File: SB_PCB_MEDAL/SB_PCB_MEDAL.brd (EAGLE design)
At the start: 60 x 60 mm, 9 parts, among them IC1 ATTINY44A-SSU

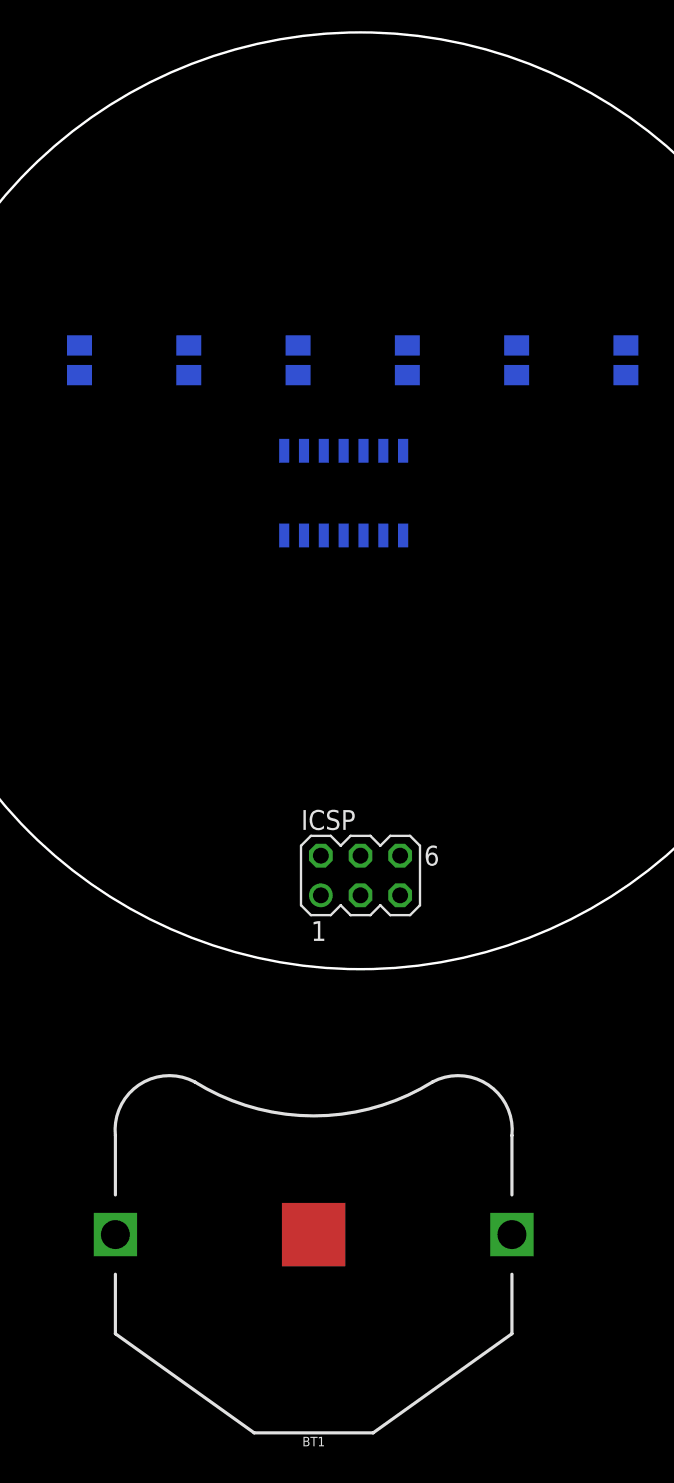
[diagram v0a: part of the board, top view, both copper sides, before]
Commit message: modified connections to button cell and added text for the ICSP header to the PCB
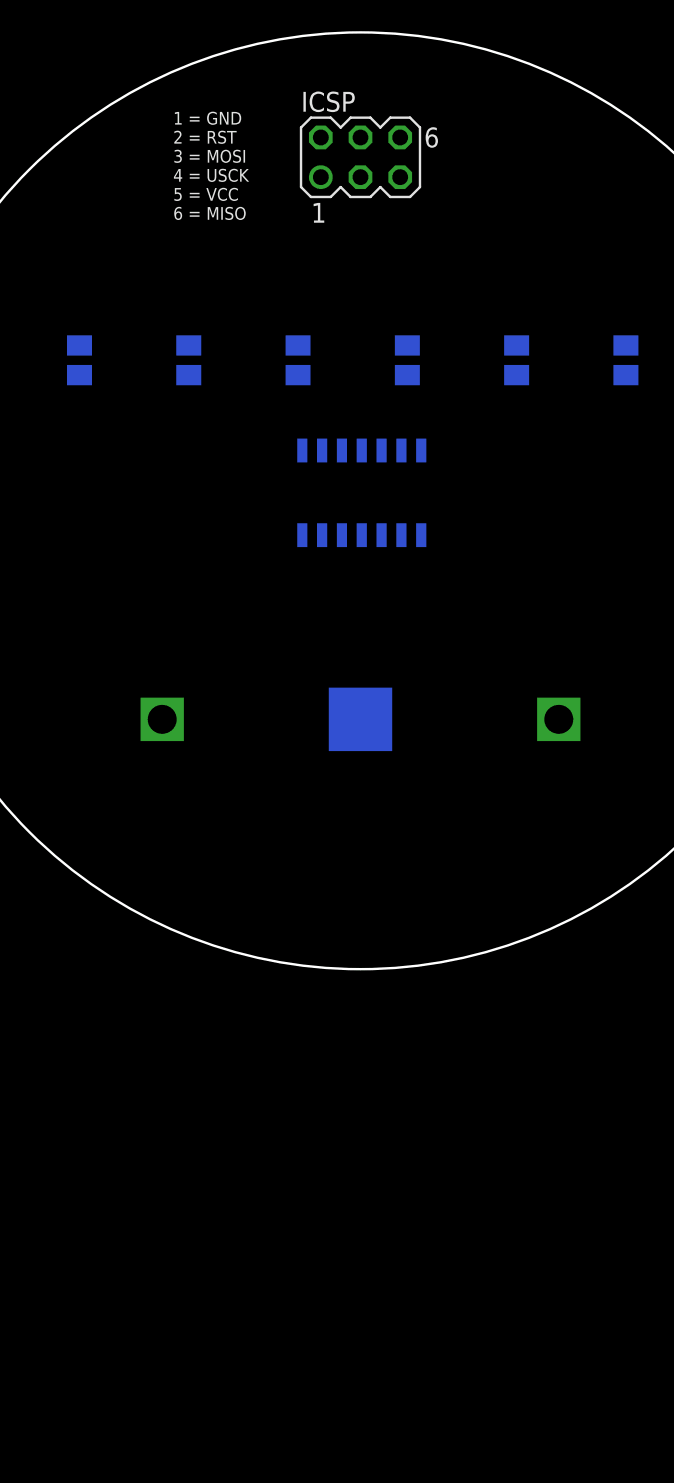
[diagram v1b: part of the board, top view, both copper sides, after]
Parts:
- moved ICSP 46.0 mm to (0.00, 22.0)
- moved BT1 33.1 mm to (0.00, -14.0), flipped to the bottom
- moved IC1 1.16 mm to (0.08, 0.51), turned to 270 degrees
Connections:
- removed net N$2: BT1.3
- net VCC: now also BT1.3
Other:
- board text added: "1 = GND 2 = RST 3 = MOSI 4 = USCK 5 = VCC 6 = MISO"
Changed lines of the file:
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@@
 <plain>
 <circle x="0" y="0" radius="30" width="0.1524" layer="20"/>
+<text x="-12" y="18" size="0.8128" layer="25">1 = GND
+2 = RST
+3 = MOSI
+4 = USCK
+5 = VCC
+6 = MISO</text>
 </plain>
 <attributes>
@@
 </autorouter>
 <elements>
-<element name="IC1" library="SamacSys_Parts" package="SOIC127P600X175-14N" value="ATTINY44A-SSU" x="-1.08" y="0.49" rot="MR90">
-<attribute name="3D_PACKAGE" value="" x="-1.08" y="0.49" size="1.778" layer="28" rot="MR90" display="off"/>
-<attribute name="ALLIED_NUMBER" value="" x="-1.08" y="0.49" size="1.778" layer="28" rot="MR90" display="off"/>
-<attribute name="DESCRIPTION" value="ATTINY44A-SSU, 8 bit AVR Microcontroller 20MHz 256 B, 4 kB Flash, 256 B RAM, I2C 14-Pin SOIC" x="-1.08" y="0.49" size="1.778" layer="28" rot="MR90" display="off"/>
-<attribute name="HEIGHT" value="1.75mm" x="-1.08" y="0.49" size="1.778" layer="28" rot="MR90" display="off"/>
-<attribute name="MANUFACTURER_NAME" value="Microchip" x="-1.08" y="0.49" size="1.778" layer="28" rot="MR90" display="off"/>
-<attribute name="MANUFACTURER_PART_NUMBER" value="ATTINY44A-SSU" x="-1.08" y="0.49" size="1.778" layer="28" rot="MR90" display="off"/>
-<attribute name="OTHER_PART_NUMBER" value="" x="-1.08" y="0.49" size="1.778" layer="28" rot="MR90" display="off"/>
-<attribute name="RS_PART_NUMBER" value="1331640P" x="-1.08" y="0.49" size="1.778" layer="28" rot="MR90" display="off"/>
-<attribute name="SUPPLIER_NAME" value="RS" x="-1.08" y="0.49" size="1.778" layer="28" rot="MR90" display="off"/>
+<element name="IC1" library="SamacSys_Parts" package="SOIC127P600X175-14N" value="ATTINY44A-SSU" x="0.08" y="0.51" rot="MR270">
+<attribute name="3D_PACKAGE" value="" x="0.08" y="0.51" size="1.778" layer="28" rot="MR270" display="off"/>
+<attribute name="ALLIED_NUMBER" value="" x="0.08" y="0.51" size="1.778" layer="28" rot="MR270" display="off"/>
+<attribute name="DESCRIPTION" value="ATTINY44A-SSU, 8 bit AVR Microcontroller 20MHz 256 B, 4 kB Flash, 256 B RAM, I2C 14-Pin SOIC" x="0.08" y="0.51" size="1.778" layer="28" rot="MR270" display="off"/>
+<attribute name="HEIGHT" value="1.75mm" x="0.08" y="0.51" size="1.778" layer="28" rot="MR270" display="off"/>
+<attribute name="MANUFACTURER_NAME" value="Microchip" x="0.08" y="0.51" size="1.778" layer="28" rot="MR270" display="off"/>
+<attribute name="MANUFACTURER_PART_NUMBER" value="ATTINY44A-SSU" x="0.08" y="0.51" size="1.778" layer="28" rot="MR270" display="off"/>
+<attribute name="OTHER_PART_NUMBER" value="" x="0.08" y="0.51" size="1.778" layer="28" rot="MR270" display="off"/>
+<attribute name="RS_PART_NUMBER" value="1331640P" x="0.08" y="0.51" size="1.778" layer="28" rot="MR270" display="off"/>
+<attribute name="SUPPLIER_NAME" value="RS" x="0.08" y="0.51" size="1.778" layer="28" rot="MR270" display="off"/>
 </element>
 <element name="R1" library="resistor" library_urn="urn:adsk.eagle:library:348" package="M0805" package3d_urn="urn:adsk.eagle:package:26079/1" value="10 Ω" x="-18" y="9" rot="MR90"/>
@@
 <element name="R5" library="resistor" library_urn="urn:adsk.eagle:library:348" package="M0805" package3d_urn="urn:adsk.eagle:package:26079/1" value="10 Ω" x="10" y="9" rot="MR90"/>
 <element name="R6" library="resistor" library_urn="urn:adsk.eagle:library:348" package="M0805" package3d_urn="urn:adsk.eagle:package:26079/1" value="10 Ω" x="17" y="9" rot="MR90"/>
-<element name="ICSP" library="con-lstb" library_urn="urn:adsk.eagle:library:162" package="MA03-2" package3d_urn="urn:adsk.eagle:package:8334/1" value="" x="0" y="-24">
-<attribute name="MF" value="" x="0" y="-24" size="1.778" layer="27" display="off"/>
-<attribute name="MPN" value="" x="0" y="-24" size="1.778" layer="27" display="off"/>
-<attribute name="OC_FARNELL" value="unknown" x="0" y="-24" size="1.778" layer="27" display="off"/>
-<attribute name="OC_NEWARK" value="unknown" x="0" y="-24" size="1.778" layer="27" display="off"/>
+<element name="ICSP" library="con-lstb" library_urn="urn:adsk.eagle:library:162" package="MA03-2" package3d_urn="urn:adsk.eagle:package:8334/1" value="" x="0" y="22">
+<attribute name="MF" value="" x="0" y="22" size="1.778" layer="27" display="off"/>
+<attribute name="MPN" value="" x="0" y="22" size="1.778" layer="27" display="off"/>
+<attribute name="OC_FARNELL" value="unknown" x="0" y="22" size="1.778" layer="27" display="off"/>
+<attribute name="OC_NEWARK" value="unknown" x="0" y="22" size="1.778" layer="27" display="off"/>
 </element>
-<element name="BT1" library="SparkFun-Batteries" library_urn="urn:adsk.eagle:library:508" package="BATTCON_24.5MM_PTH" package3d_urn="urn:adsk.eagle:package:37222/1" value="" x="-3" y="-47">
-<attribute name="SF_SKU" value="PRT-08863" x="-3" y="-47" size="1.778" layer="27" display="off"/>
+<element name="BT1" library="SparkFun-Batteries" library_urn="urn:adsk.eagle:library:508" package="BATTCON_24.5MM_PTH" package3d_urn="urn:adsk.eagle:package:37222/1" value="" x="0" y="-14" rot="MR0">
+<attribute name="SF_SKU" value="PRT-08863" x="0" y="-14" size="1.778" layer="28" rot="MR0" display="off"/>
 </element>
 </elements>
 <signals>
 <signal name="VCC">
+<contactref element="IC1" pad="1"/>
 <contactref element="ICSP" pad="5"/>
-<contactref element="IC1" pad="1"/>
-<wire x1="2.73" y1="-2.221" x2="2.54" y2="-25.27" width="0" layer="19" extent="16-16"/>
+<contactref element="BT1" pad="3"/>
+<wire x1="-3.73" y1="3.221" x2="-12.7" y2="-14" width="0" layer="19" extent="16-16"/>
+<wire x1="2.54" y1="20.73" x2="-3.73" y2="3.221" width="0" layer="19" extent="16-16"/>
 </signal>
 <signal name="GND">
-<contactref element="IC1" pad="14"/>
 <contactref element="ICSP" pad="1"/>
 <contactref element="BT1" pad="2"/>
-<wire x1="-2.54" y1="-25.27" x2="-3" y2="-47" width="0" layer="19" extent="1-1"/>
-<wire x1="2.73" y1="3.201" x2="-2.54" y2="-25.27" width="0" layer="19" extent="16-16"/>
+<contactref element="IC1" pad="14"/>
+<wire x1="-3.73" y1="-2.201" x2="-2.54" y2="20.73" width="0" layer="19" extent="16-16"/>
+<wire x1="0" y1="-14" x2="-3.73" y2="-2.201" width="0" layer="19" extent="16-16"/>
 </signal>
 <signal name="MISO">
 <contactref element="ICSP" pad="6"/>
 <contactref element="IC1" pad="8"/>
-<wire x1="-4.89" y1="3.201" x2="2.54" y2="-22.73" width="0" layer="19" extent="16-16"/>
+<wire x1="3.89" y1="-2.201" x2="2.54" y2="23.27" width="0" layer="19" extent="16-16"/>
 </signal>
 <signal name="MOSI">
 <contactref element="IC1" pad="7"/>
 <contactref element="ICSP" pad="3"/>
-<wire x1="-4.89" y1="-2.221" x2="0" y2="-25.27" width="0" layer="19" extent="16-16"/>
+<wire x1="3.89" y1="3.221" x2="0" y2="20.73" width="0" layer="19" extent="16-16"/>
 </signal>
 <signal name="RST">
 <contactref element="IC1" pad="4"/>
 <contactref element="ICSP" pad="2"/>
-<wire x1="-1.08" y1="-2.221" x2="-2.54" y2="-22.73" width="0" layer="19" extent="16-16"/>
+<wire x1="0.08" y1="3.221" x2="-2.54" y2="23.27" width="0" layer="19" extent="16-16"/>
 </signal>
 <signal name="USCK">
 <contactref element="IC1" pad="9"/>
 <contactref element="ICSP" pad="4"/>
-<wire x1="-3.62" y1="3.201" x2="0" y2="-22.73" width="0" layer="19" extent="16-16"/>
-</signal>
-<signal name="N$2">
-<contactref element="BT1" pad="3"/>
+<wire x1="2.62" y1="-2.201" x2="0" y2="23.27" width="0" layer="19" extent="16-16"/>
 </signal>
 </signals>
@@
 </drawing>
 <compatibility>
+<note version="6.3" minversion="6.2.2" severity="warning">
+Since Version 6.2.2 text objects can contain more than one line,
+which will not be processed correctly with this version.
+</note>
 <note version="8.2" severity="warning">
 Since Version 8.2, EAGLE supports online libraries. The ids

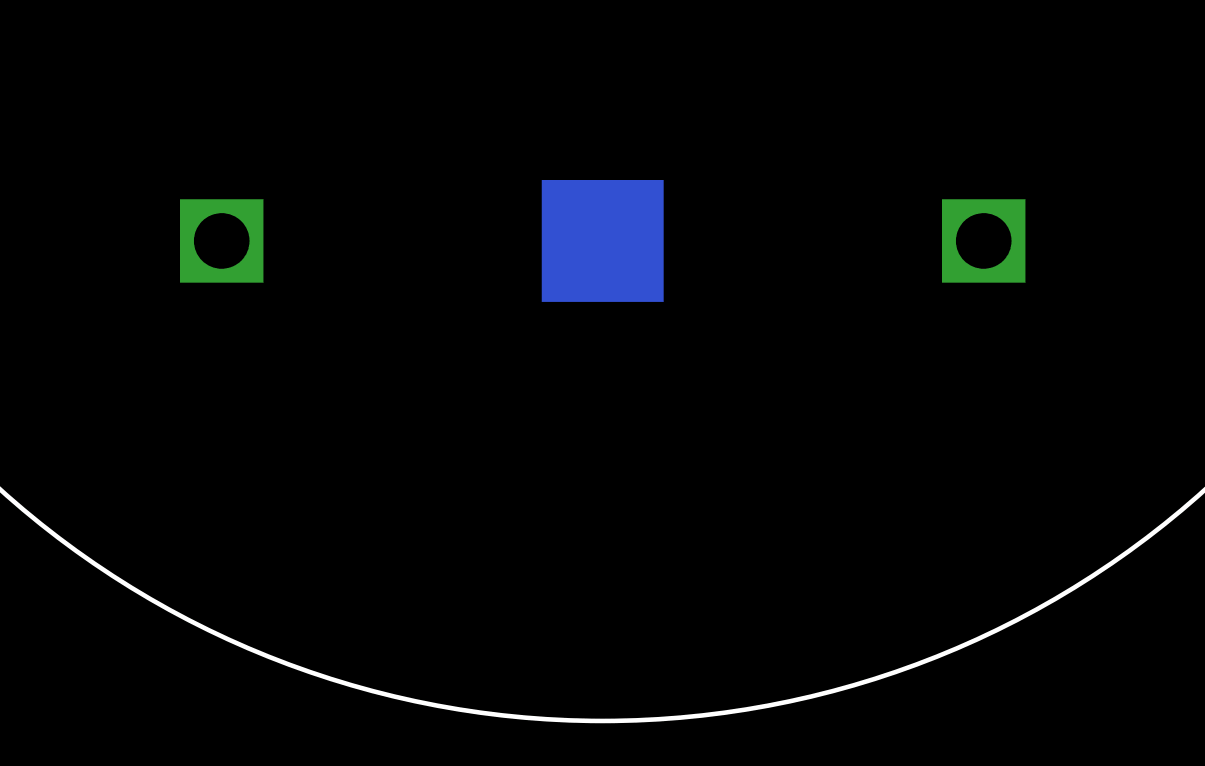
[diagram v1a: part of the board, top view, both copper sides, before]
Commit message: removed 24mm button cell from schematic and replaced with smaller 12mm due to size issues on the board
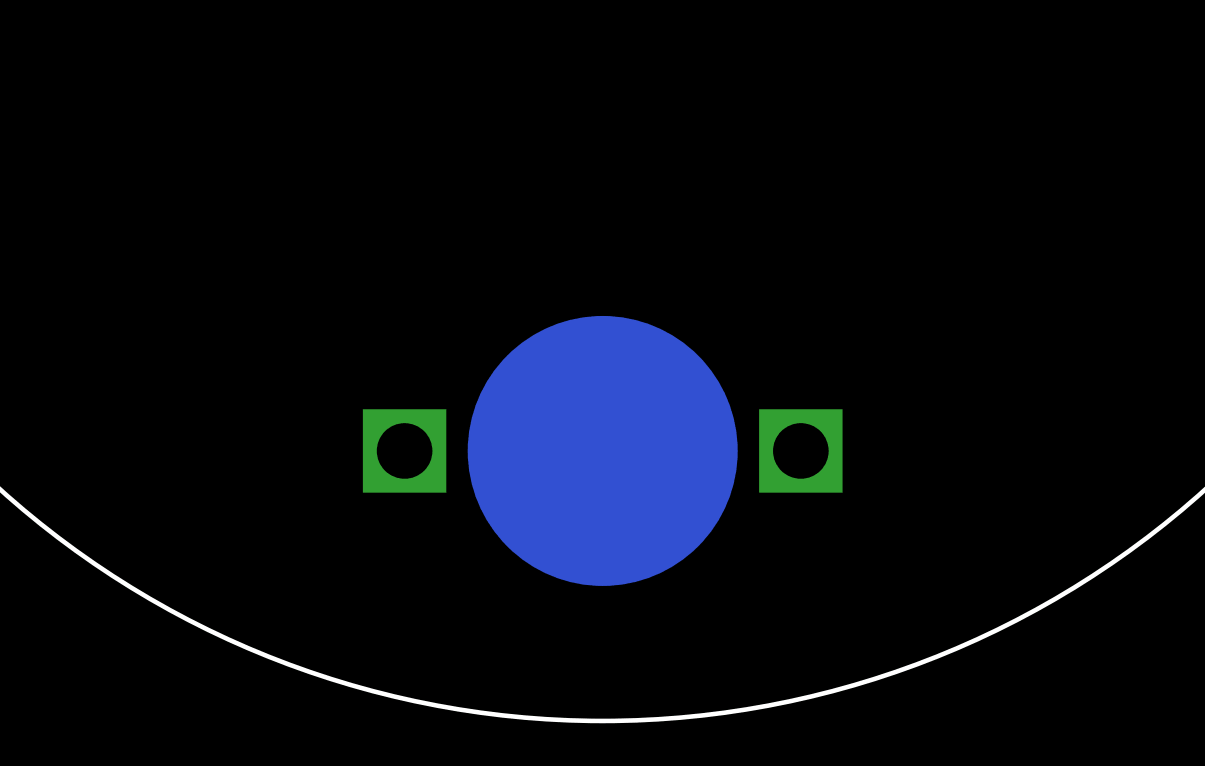
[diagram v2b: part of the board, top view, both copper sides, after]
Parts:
- BT1: device SparkFun-Batteries:BATTCON_24.5MM_PTH -> SparkFun-Batteries:BATTCON_12MM_PTH
- moved BT1 7.00 mm to (0.00, -21.0)
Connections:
- net GND: now also BT1.GND; no longer BT1.2
- net VCC: now also BT1.VCC@1; no longer BT1.3
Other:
- board text added: "Schematic and PCB by: Anton Nikitin Henry Oliver-Edwards"
- board text added: "SourceBots 2018"
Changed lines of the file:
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@@
 5 = VCC
 6 = MISO</text>
+<text x="11" y="13" size="1.9304" layer="26" rot="MR0">SourceBots 2018</text>
+<text x="-6" y="-1" size="0.4064" layer="26" rot="MR0">Schematic and PCB by:
+Anton Nikitin
+Henry Oliver-Edwards
+</text>
 </plain>
 <attributes>
@@
 <attribute name="OC_NEWARK" value="unknown" x="0" y="22" size="1.778" layer="27" display="off"/>
 </element>
-<element name="BT1" library="SparkFun-Batteries" library_urn="urn:adsk.eagle:library:508" package="BATTCON_24.5MM_PTH" package3d_urn="urn:adsk.eagle:package:37222/1" value="" x="0" y="-14" rot="MR0">
-<attribute name="SF_SKU" value="PRT-08863" x="0" y="-14" size="1.778" layer="28" rot="MR0" display="off"/>
+<element name="BT1" library="SparkFun-Batteries" library_urn="urn:adsk.eagle:library:508" package="BATTCON_12MM_PTH" package3d_urn="urn:adsk.eagle:package:37213/1" value="" x="0" y="-21" rot="MR0">
+<attribute name="PROD_ID" value="BATT-08315" x="0" y="-21" size="0.4064" layer="28" rot="MR0" display="off"/>
+<attribute name="SF_SKU" value="PRT-07948" x="0" y="-21" size="0.4064" layer="28" rot="MR0" display="off"/>
 </element>
 </elements>
@@
 <contactref element="IC1" pad="1"/>
 <contactref element="ICSP" pad="5"/>
-<contactref element="BT1" pad="3"/>
-<wire x1="-3.73" y1="3.221" x2="-12.7" y2="-14" width="0" layer="19" extent="16-16"/>
+<contactref element="BT1" pad="VCC@1"/>
+<wire x1="-3.73" y1="3.221" x2="-6.604" y2="-21" width="0" layer="19" extent="16-16"/>
 <wire x1="2.54" y1="20.73" x2="-3.73" y2="3.221" width="0" layer="19" extent="16-16"/>
 </signal>
 <signal name="GND">
 <contactref element="ICSP" pad="1"/>
-<contactref element="BT1" pad="2"/>
 <contactref element="IC1" pad="14"/>
-<wire x1="-3.73" y1="-2.201" x2="-2.54" y2="20.73" width="0" layer="19" extent="16-16"/>
-<wire x1="0" y1="-14" x2="-3.73" y2="-2.201" width="0" layer="19" extent="16-16"/>
+<contactref element="BT1" pad="GND"/>
+<wire x1="-3.73" y1="-2.201" x2="0" y2="-21" width="0" layer="19" extent="1-16"/>
+<wire x1="-2.54" y1="20.73" x2="-3.73" y2="-2.201" width="0" layer="19" extent="16-16"/>
 </signal>
 <signal name="MISO">

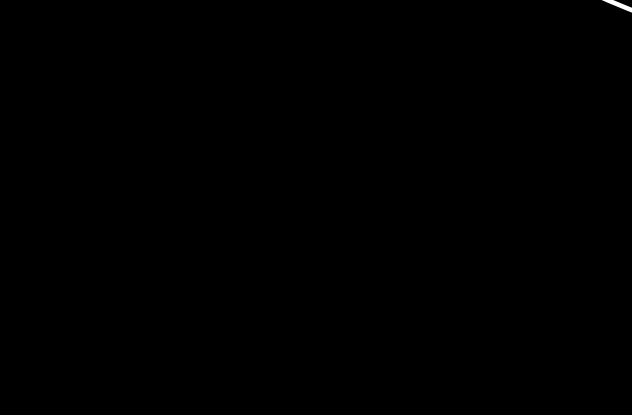
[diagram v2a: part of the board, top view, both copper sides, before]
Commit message: added one LED to the schematic
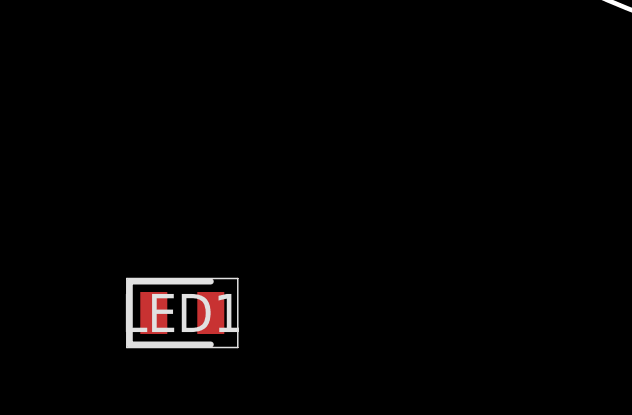
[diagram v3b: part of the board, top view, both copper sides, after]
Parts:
- added LED1: KPT-2012CGCK, SamacSys_Parts:LEDC2012X78N
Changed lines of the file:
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@@
 <attribute name="SF_SKU" value="PRT-07948" x="0" y="-21" size="0.4064" layer="28" rot="MR0" display="off"/>
+</element>
+<element name="LED1" library="SamacSys_Parts" package="LEDC2012X78N" value="KPT-2012CGCK" x="-26" y="-38">
+<attribute name="3D_PACKAGE" value="" x="-26" y="-38" size="1.778" layer="27" display="off"/>
+<attribute name="ALLIED_NUMBER" value="" x="-26" y="-38" size="1.778" layer="27" display="off"/>
+<attribute name="DESCRIPTION" value="Green Chip LED 2x1.25mm Kingbright KPT-2012CGCK Green LED, 570 nm, 2012 (0805), Rectangle Lens SMD Package" x="-26" y="-38" size="1.778" layer="27" display="off"/>
+<attribute name="HEIGHT" value="0.78mm" x="-26" y="-38" size="1.778" layer="27" display="off"/>
+<attribute name="MANUFACTURER_NAME" value="Kingbright" x="-26" y="-38" size="1.778" layer="27" display="off"/>
+<attribute name="MANUFACTURER_PART_NUMBER" value="KPT-2012CGCK" x="-26" y="-38" size="1.778" layer="27" display="off"/>
+<attribute name="OTHER_PART_NUMBER" value="" x="-26" y="-38" size="1.778" layer="27" display="off"/>
+<attribute name="RS_PART_NUMBER" value="8610172P" x="-26" y="-38" size="1.778" layer="27" display="off"/>
+<attribute name="SUPPLIER_NAME" value="RS" x="-26" y="-38" size="1.778" layer="27" display="off"/>
 </element>
 </elements>
